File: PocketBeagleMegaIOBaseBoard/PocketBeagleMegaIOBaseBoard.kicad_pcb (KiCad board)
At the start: 2 copper layers, 45.7 x 174 mm, 40 parts, among them J1 RJ45, J2 RJ45, P1 POCKETBEAGLE-P1, P101 0 1, P2 POCKETBEAGLE-P2, P201 GPIO 3, P202 GPIO 4, P301 GPIO 5, P302 GPIO 6, T1 + 15 in -, T2 + 15 out -, U1 TCAN332DR, U2 SN65HVD233-HT, U201 MCP23017, U3 LM2574N-5.0, U301 MCP23017

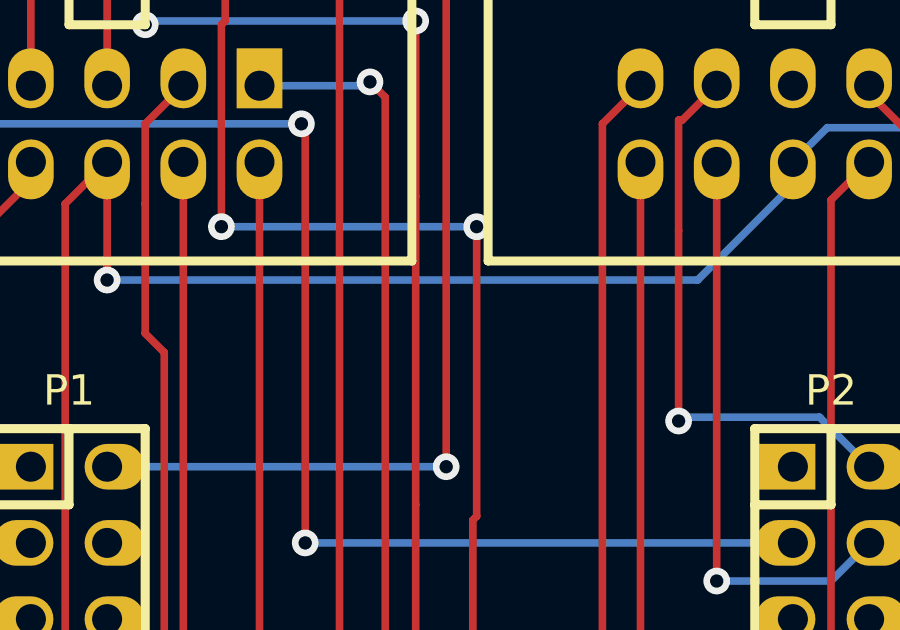
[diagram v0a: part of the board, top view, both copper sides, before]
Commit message: Mark orientation of ESP32 and PocketBeagle modules on the silk.
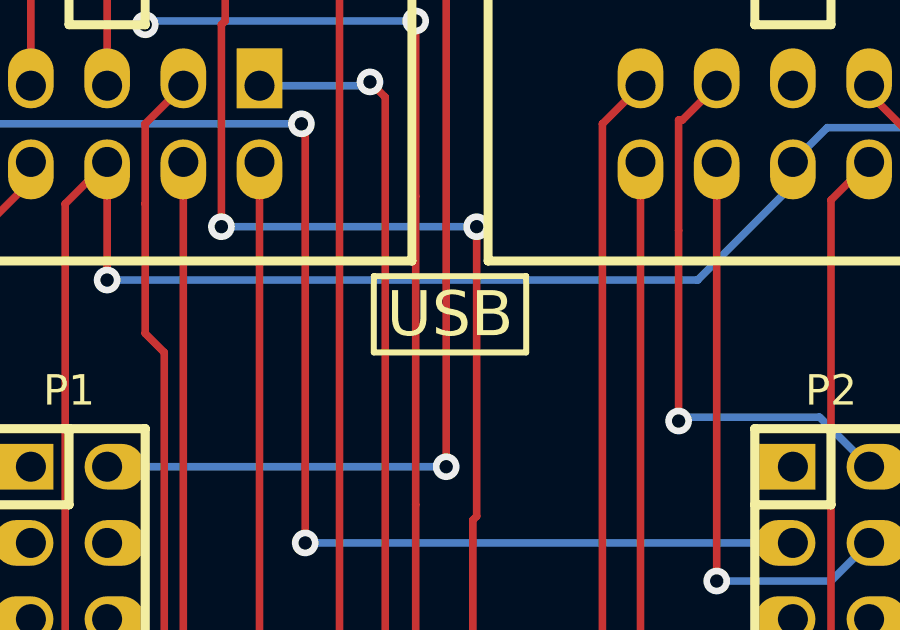
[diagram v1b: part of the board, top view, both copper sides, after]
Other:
- board text added: "USB"
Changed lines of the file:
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@@
     (area 89.015994 24.606956 190.582126 202.88758)
     (thickness 1.6)
-    (drawings 4)
+    (drawings 9)
     (tracks 591)
     (zones 0)
@@
     (19 F.Paste user)
     (20 B.SilkS user)
-    (21 F.SilkS user hide)
+    (21 F.SilkS user)
     (22 B.Mask user)
     (23 F.Mask user)
@@
     )
   )
+  (gr_line (start 142.24 91.44) (end 137.16 91.44) (angle 90) (layer F.SilkS) (width 0.2))
+  (gr_line (start 142.24 93.98) (end 142.24 91.44) (angle 90) (layer F.SilkS) (width 0.2))
+  (gr_line (start 137.16 93.98) (end 142.24 93.98) (angle 90) (layer F.SilkS) (width 0.2))
+  (gr_line (start 137.16 91.44) (end 137.16 93.98) (angle 90) (layer F.SilkS) (width 0.2))
+  (gr_text USB (at 139.7 92.71) (layer F.SilkS)
+    (effects (font (size 1.5 1.5) (thickness 0.3)))
+  )
   (gr_line (start 162.56 27.94) (end 162.56 201.93) (angle 90) (layer Edge.Cuts) (width 0.1))

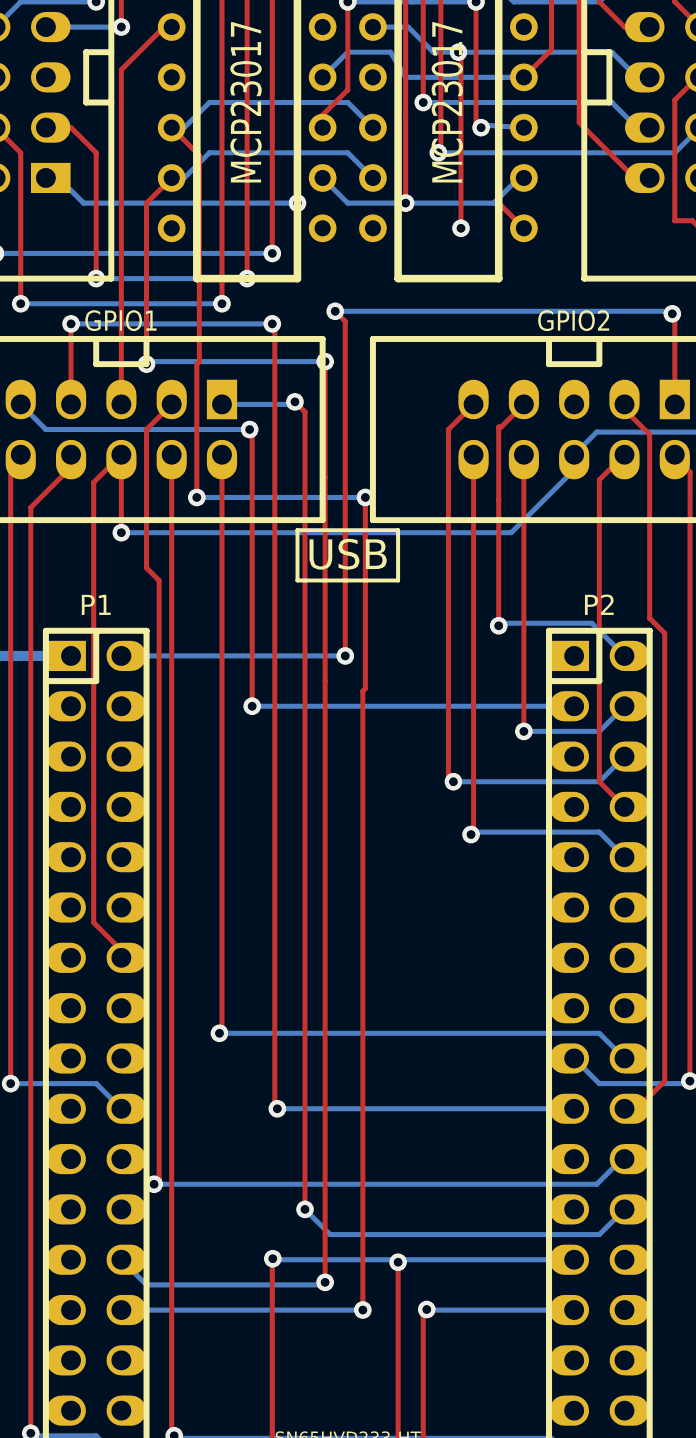
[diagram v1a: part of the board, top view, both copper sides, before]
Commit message: Move from I2C2 to I2C1 (reserve I2C2 for eeprom.
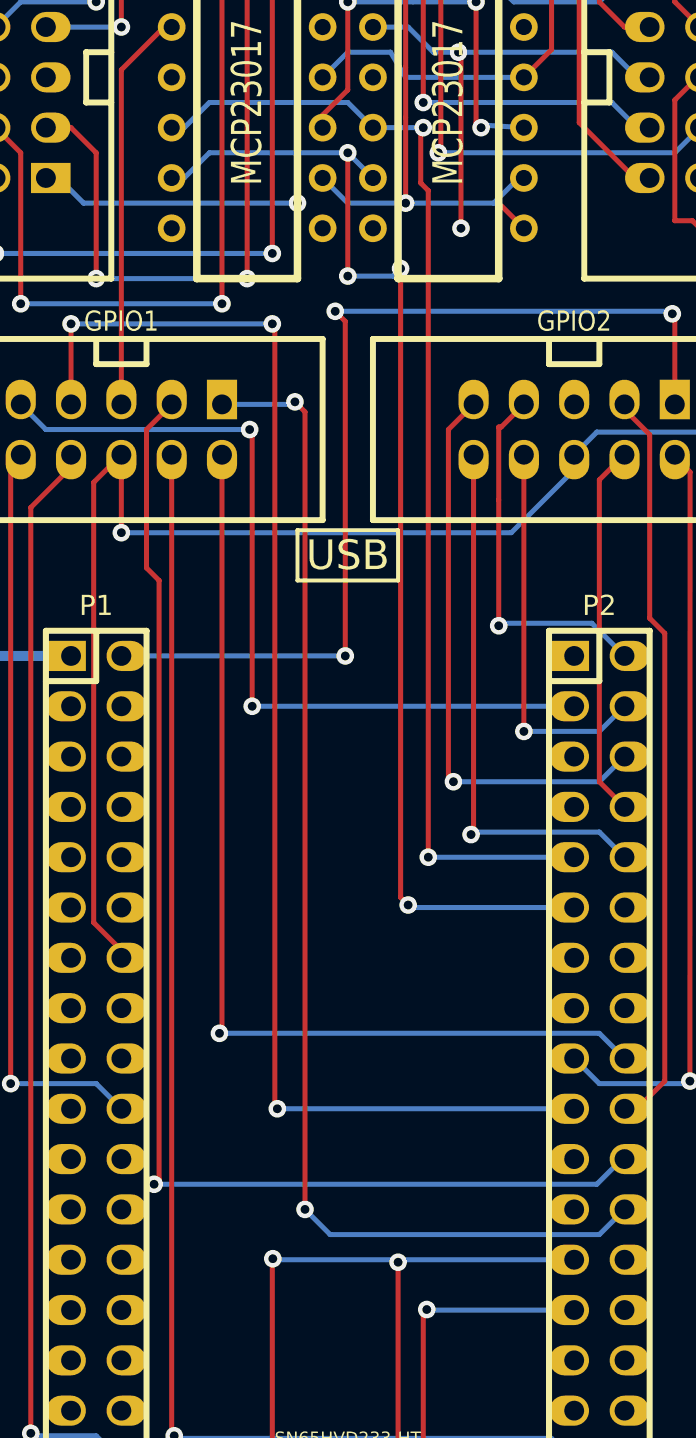
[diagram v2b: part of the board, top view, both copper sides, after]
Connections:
- P1 pad 26: /MCP23017 1/SDA -> (no net)
- P1 pad 28: /MCP23017 1/SCL -> (no net)
- P2 pad 11: (no net) -> /MCP23017 1/SDA
- P2 pad 9: (no net) -> /MCP23017 1/SCL
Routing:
- net /MCP23017 1/SCL: track 92.3 -> 58.2 mm, vias 3 -> 2
- net /MCP23017 1/SDA: track 87.8 -> 61.1 mm, vias 3 -> 4
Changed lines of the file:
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@@
     (thickness 1.6)
     (drawings 9)
-    (tracks 591)
+    (tracks 585)
     (zones 0)
     (modules 40)
@@
     (pad 26 thru_hole oval (at 8.89 -1.27 270) (size 1.524 1.99898) (drill 1.00076 (offset 0 -0.24892))
       (layers *.Cu *.Mask F.SilkS)
-      (net 26 "/MCP23017 1/SDA")
     )
     (pad 27 thru_hole oval (at 11.43 1.27 270) (size 1.524 1.99898) (drill 1.00076 (offset 0 0.24892))
@@
     (pad 28 thru_hole oval (at 11.43 -1.27 270) (size 1.524 1.99898) (drill 1.00076 (offset 0 -0.24892))
       (layers *.Cu *.Mask F.SilkS)
-      (net 25 "/MCP23017 1/SCL")
     )
     (pad 29 thru_hole oval (at 13.97 1.27 270) (size 1.524 1.99898) (drill 1.00076 (offset 0 0.24892))
@@
     (pad 9 thru_hole oval (at -11.43 1.27 270) (size 1.524 1.99898) (drill 1.00076 (offset 0 0.24892))
       (layers *.Cu *.Mask F.SilkS)
+      (net 25 "/MCP23017 1/SCL")
     )
     (pad 10 thru_hole oval (at -11.43 -1.27 270) (size 1.524 1.99898) (drill 1.00076 (offset 0 -0.24892))
@@
     (pad 11 thru_hole oval (at -8.89 1.27 270) (size 1.524 1.99898) (drill 1.00076 (offset 0 0.24892))
       (layers *.Cu *.Mask F.SilkS)
+      (net 26 "/MCP23017 1/SDA")
     )
     (pad 12 thru_hole oval (at -8.89 -1.27 270) (size 1.524 1.99898) (drill 1.00076 (offset 0 -0.24892))
@@
   (segment (start 139.7 67.31) (end 141.859 67.31) (width 0.254) (layer B.Cu) (net 24))
   (segment (start 141.859 67.31) (end 142.621 68.58) (width 0.254) (layer B.Cu) (net 24))
-  (segment (start 130.81 71.12) (end 132.207 72.517) (width 0.254) (layer F.Cu) (net 25))
-  (segment (start 140.462 130.81) (end 128.27 130.81) (width 0.254) (layer B.Cu) (net 25))
-  (via (at 140.462 130.81) (size 0.889) (layers F.Cu B.Cu) (net 25))
-  (segment (start 140.462 99.568) (end 140.462 130.81) (width 0.254) (layer F.Cu) (net 25))
-  (segment (start 140.589 99.441) (end 140.462 99.568) (width 0.254) (layer F.Cu) (net 25))
-  (segment (start 140.589 89.789) (end 140.589 99.441) (width 0.254) (layer F.Cu) (net 25))
-  (via (at 140.589 89.789) (size 0.889) (layers F.Cu B.Cu) (net 25))
-  (segment (start 132.08 89.789) (end 140.589 89.789) (width 0.254) (layer B.Cu) (net 25))
-  (via (at 132.08 89.789) (size 0.889) (layers F.Cu B.Cu) (net 25))
-  (segment (start 132.08 83.058) (end 132.08 89.789) (width 0.254) (layer F.Cu) (net 25))
-  (segment (start 132.207 82.931) (end 132.08 83.058) (width 0.254) (layer F.Cu) (net 25))
-  (segment (start 132.207 72.517) (end 132.207 82.931) (width 0.254) (layer F.Cu) (net 25))
+  (segment (start 140.97 71.12) (end 143.51 71.12) (width 0.254) (layer B.Cu) (net 25))
+  (segment (start 143.764 107.95) (end 151.13 107.95) (width 0.254) (layer B.Cu) (net 25))
+  (via (at 143.764 107.95) (size 0.889) (layers F.Cu B.Cu) (net 25))
+  (segment (start 143.764 74.295) (end 143.764 107.95) (width 0.254) (layer F.Cu) (net 25))
+  (segment (start 143.383 73.914) (end 143.764 74.295) (width 0.254) (layer F.Cu) (net 25))
+  (segment (start 143.383 71.247) (end 143.383 73.914) (width 0.254) (layer F.Cu) (net 25))
+  (segment (start 143.51 71.12) (end 143.383 71.247) (width 0.254) (layer F.Cu) (net 25))
+  (via (at 143.51 71.12) (size 0.889) (layers F.Cu B.Cu) (net 25))
   (segment (start 140.97 71.12) (end 139.7 69.85) (width 0.254) (layer B.Cu) (net 25))
   (segment (start 131.445 71.12) (end 130.81 71.12) (width 0.254) (layer B.Cu) (net 25))
   (segment (start 132.715 69.85) (end 131.445 71.12) (width 0.254) (layer B.Cu) (net 25))
   (segment (start 139.7 69.85) (end 132.715 69.85) (width 0.254) (layer B.Cu) (net 25))
-  (segment (start 130.81 73.66) (end 129.54 74.93) (width 0.254) (layer F.Cu) (net 26))
-  (segment (start 129.54 129.54) (end 128.27 128.27) (width 0.254) (layer B.Cu) (net 26))
-  (segment (start 138.43 129.54) (end 129.54 129.54) (width 0.254) (layer B.Cu) (net 26))
-  (segment (start 138.557 129.413) (end 138.43 129.54) (width 0.254) (layer B.Cu) (net 26))
-  (via (at 138.557 129.413) (size 0.889) (layers F.Cu B.Cu) (net 26))
-  (segment (start 138.557 99.06) (end 138.557 129.413) (width 0.254) (layer F.Cu) (net 26))
-  (segment (start 138.557 88.773) (end 138.557 99.06) (width 0.254) (layer F.Cu) (net 26))
-  (segment (start 138.557 82.931) (end 138.557 88.773) (width 0.254) (layer F.Cu) (net 26))
-  (via (at 138.557 82.931) (size 0.889) (layers F.Cu B.Cu) (net 26))
-  (segment (start 129.413 82.931) (end 138.557 82.931) (width 0.254) (layer B.Cu) (net 26))
-  (segment (start 129.54 83.058) (end 129.413 82.931) (width 0.254) (layer B.Cu) (net 26))
-  (via (at 129.54 83.058) (size 0.889) (layers F.Cu B.Cu) (net 26))
-  (segment (start 129.54 74.93) (end 129.54 83.058) (width 0.254) (layer F.Cu) (net 26))
+  (segment (start 151.13 110.49) (end 142.748 110.49) (width 0.254) (layer B.Cu) (net 26))
+  (via (at 139.7 72.39) (size 0.889) (layers F.Cu B.Cu) (net 26))
+  (segment (start 139.7 78.613) (end 139.7 72.39) (width 0.254) (layer F.Cu) (net 26))
+  (via (at 139.7 78.613) (size 0.889) (layers F.Cu B.Cu) (net 26))
+  (segment (start 141.986 78.613) (end 139.7 78.613) (width 0.254) (layer B.Cu) (net 26))
+  (segment (start 142.367 78.232) (end 141.986 78.613) (width 0.254) (layer B.Cu) (net 26))
+  (via (at 142.367 78.232) (size 0.889) (layers F.Cu B.Cu) (net 26))
+  (segment (start 142.367 109.982) (end 142.367 78.232) (width 0.254) (layer F.Cu) (net 26))
+  (segment (start 142.748 110.363) (end 142.367 109.982) (width 0.254) (layer F.Cu) (net 26))
+  (via (at 142.748 110.363) (size 0.889) (layers F.Cu B.Cu) (net 26))
+  (segment (start 142.748 110.49) (end 142.748 110.363) (width 0.254) (layer B.Cu) (net 26))
   (segment (start 130.81 73.66) (end 131.445 73.66) (width 0.254) (layer B.Cu) (net 26))
   (segment (start 139.7 72.39) (end 140.97 73.66) (width 0.254) (layer B.Cu) (net 26))

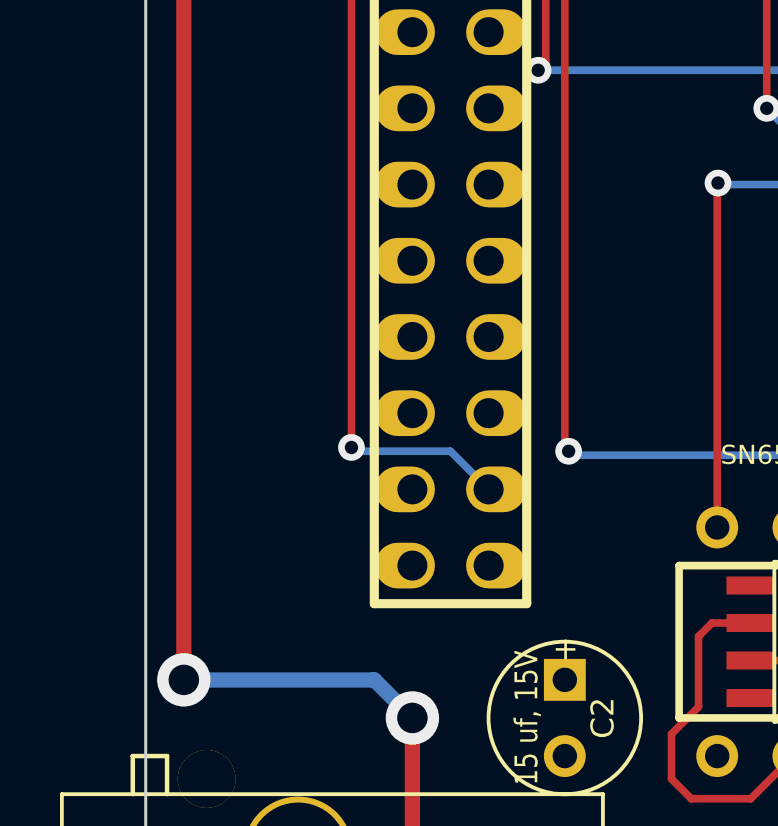
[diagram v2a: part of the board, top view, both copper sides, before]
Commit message: Add Console headers to all Pocket Beagle boards.
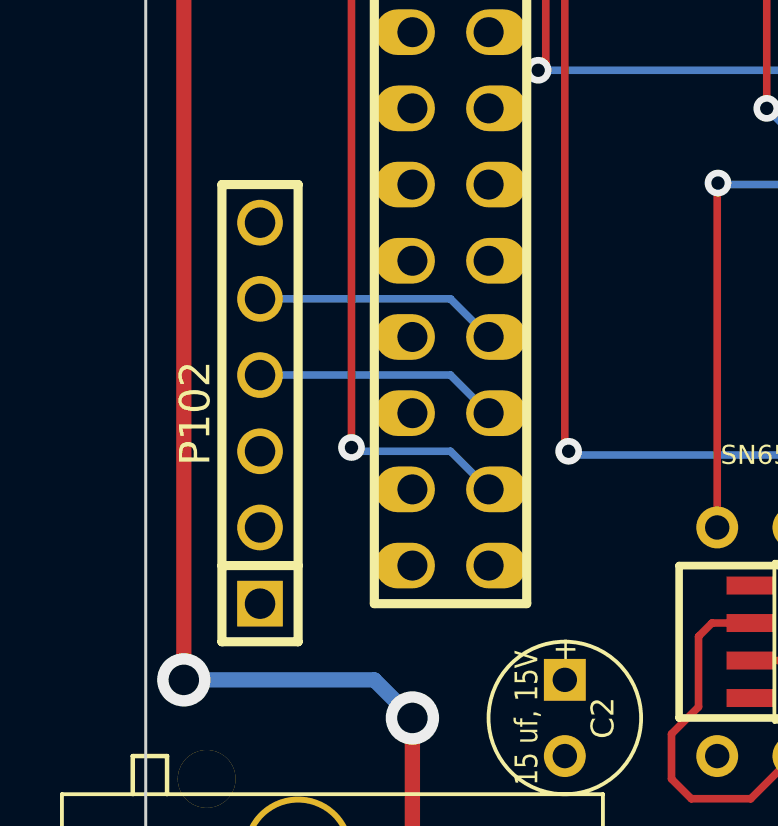
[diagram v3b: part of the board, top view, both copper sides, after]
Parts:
- added P102: Console, PIN_ARRAY-6X1, F.Cu at (120.7, 135.9)
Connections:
- P1 pad 30: (no net) -> N-0000013
- P1 pad 32: (no net) -> N-0000012
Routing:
- net N-0000013: track 0.00 -> 8.15 mm
- net N-0000012: track 0.00 -> 8.15 mm
